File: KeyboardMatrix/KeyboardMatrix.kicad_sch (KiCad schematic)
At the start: 19 parts

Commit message: Updated schematic page details
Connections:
- net at Arduino-Due-Conn. (GND): now also Keyboard Conn1. (GND)
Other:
- title: (none) -> Keyboard Matrix
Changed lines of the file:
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@@
 	(generator_version "8.0")
 	(paper "A4")
+	(title_block
+		(title "Keyboard Matrix")
+		(date "2024-09-20")
+	)
 	(junction
 		(at 184.15 100.33)

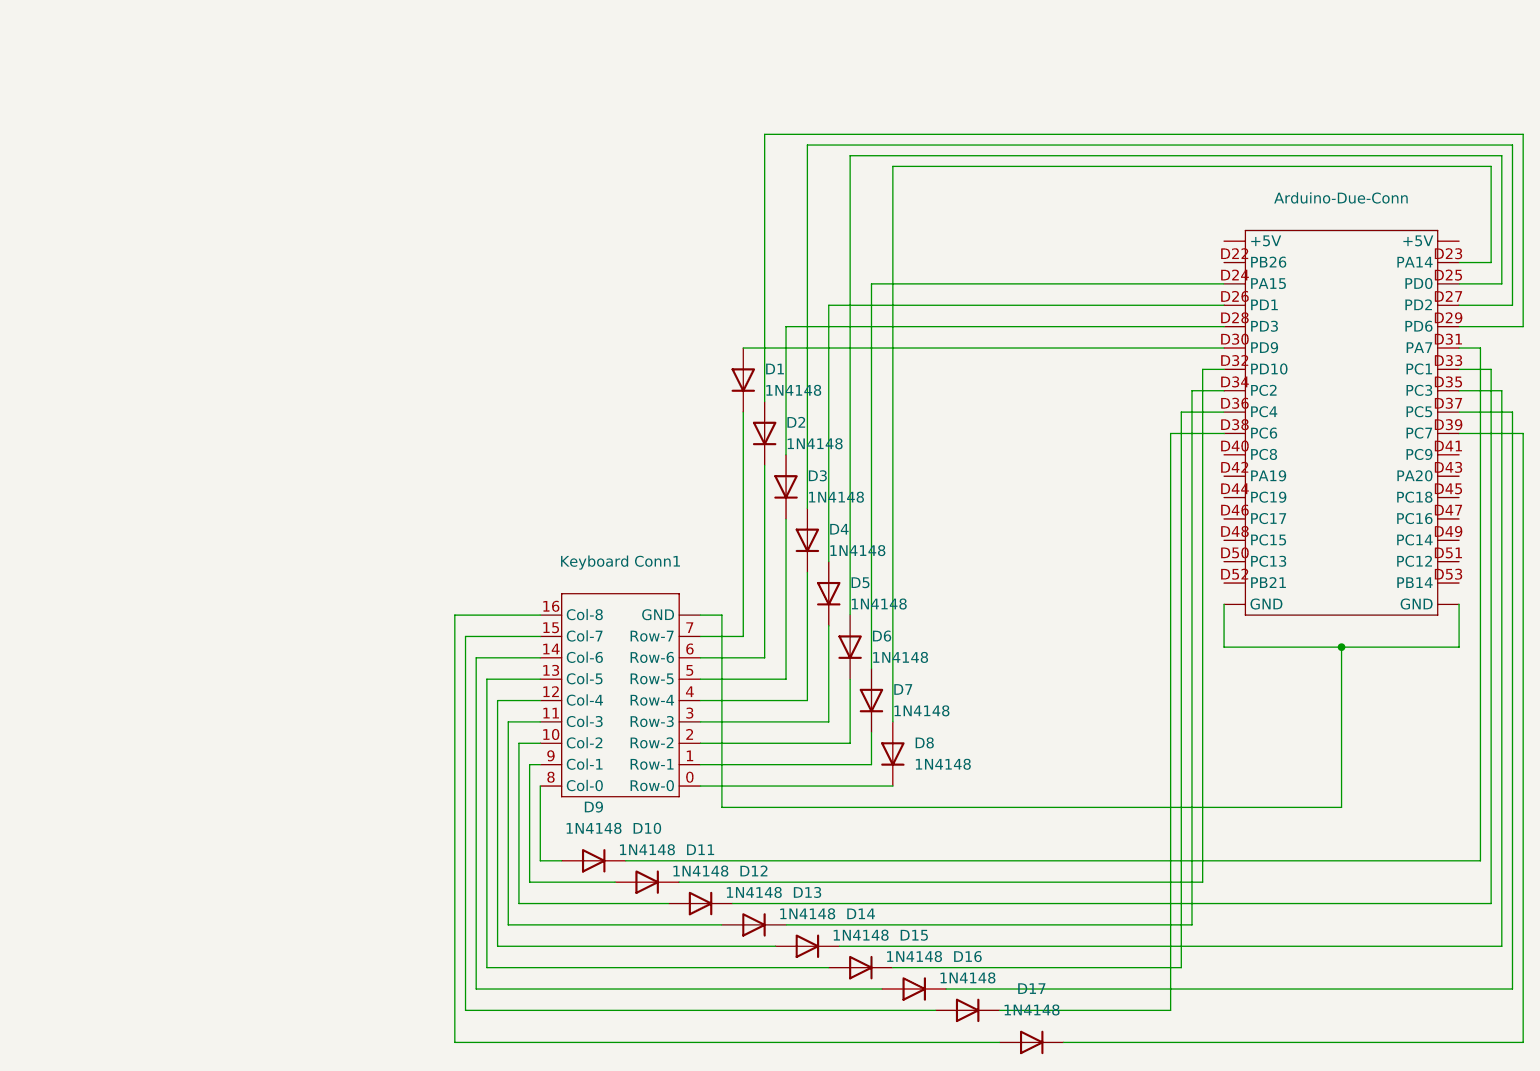
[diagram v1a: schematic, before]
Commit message: Changed schematic page size
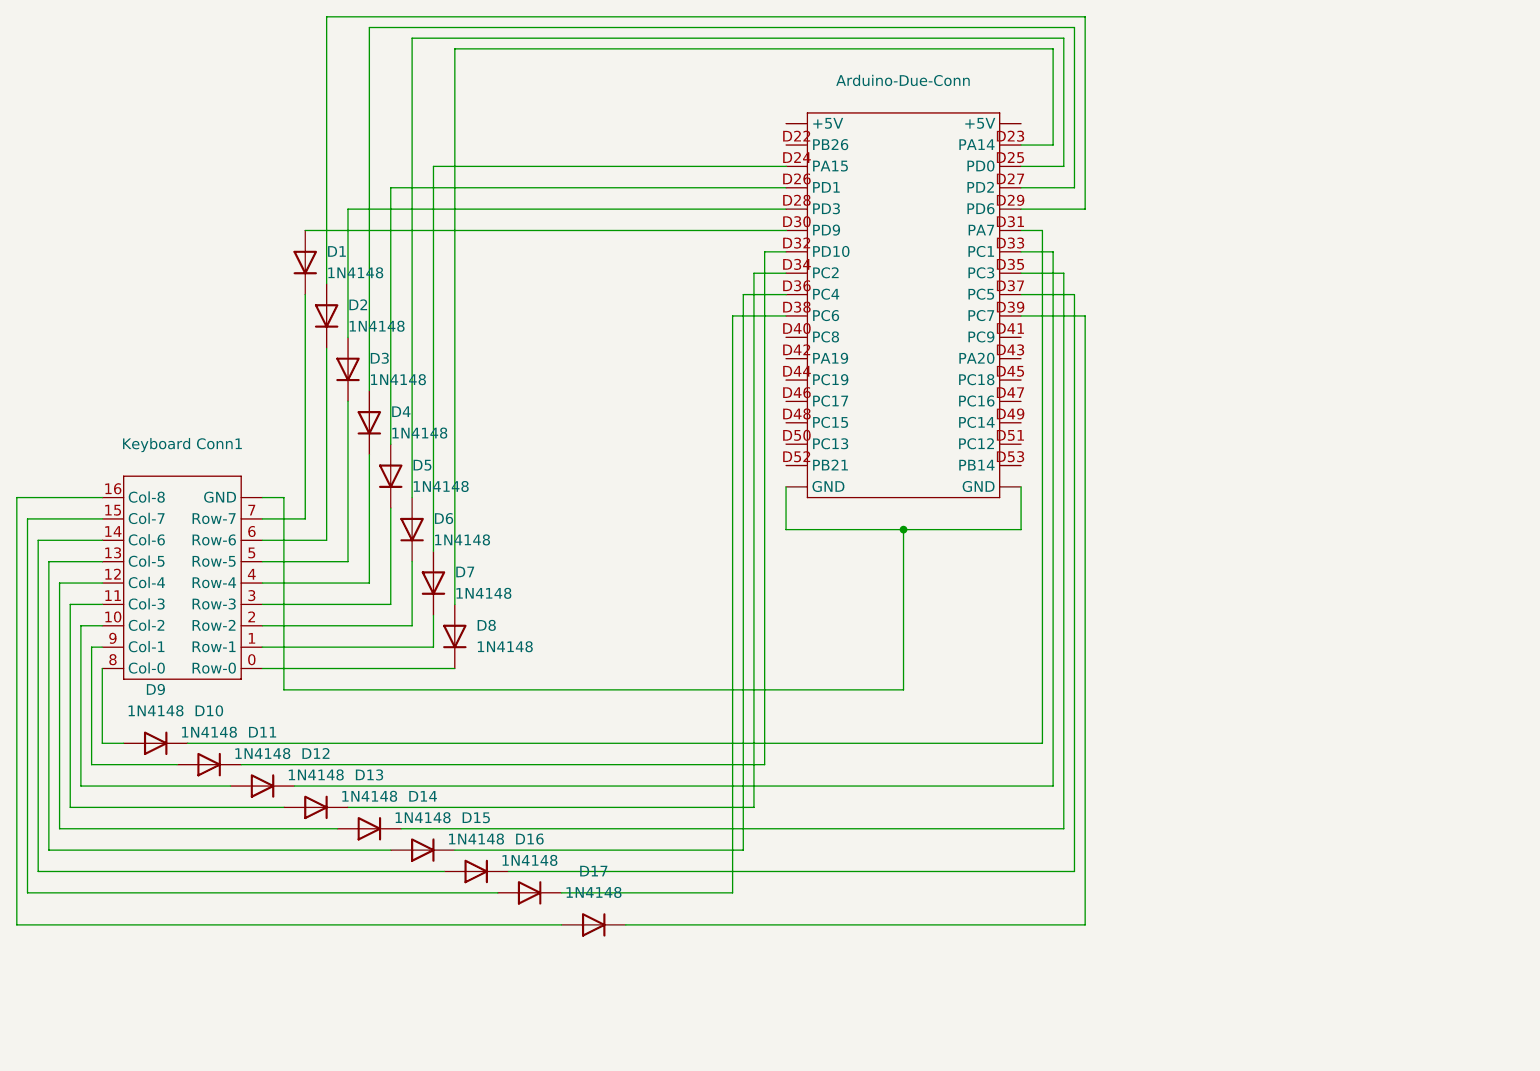
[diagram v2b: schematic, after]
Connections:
- net at Arduino-Due-Conn. (GND): now also Keyboard Conn1. (GND)
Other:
- moved on the sheet: Arduino-Due-Conn, D1, D10, D11, D12, D13, D14, D15, D16, D17, D2, D3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
